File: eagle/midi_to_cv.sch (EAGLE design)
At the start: 46 parts, among them IC1 TL084P, IC2 TL084P, U1 ATMEGA328P_PDIP

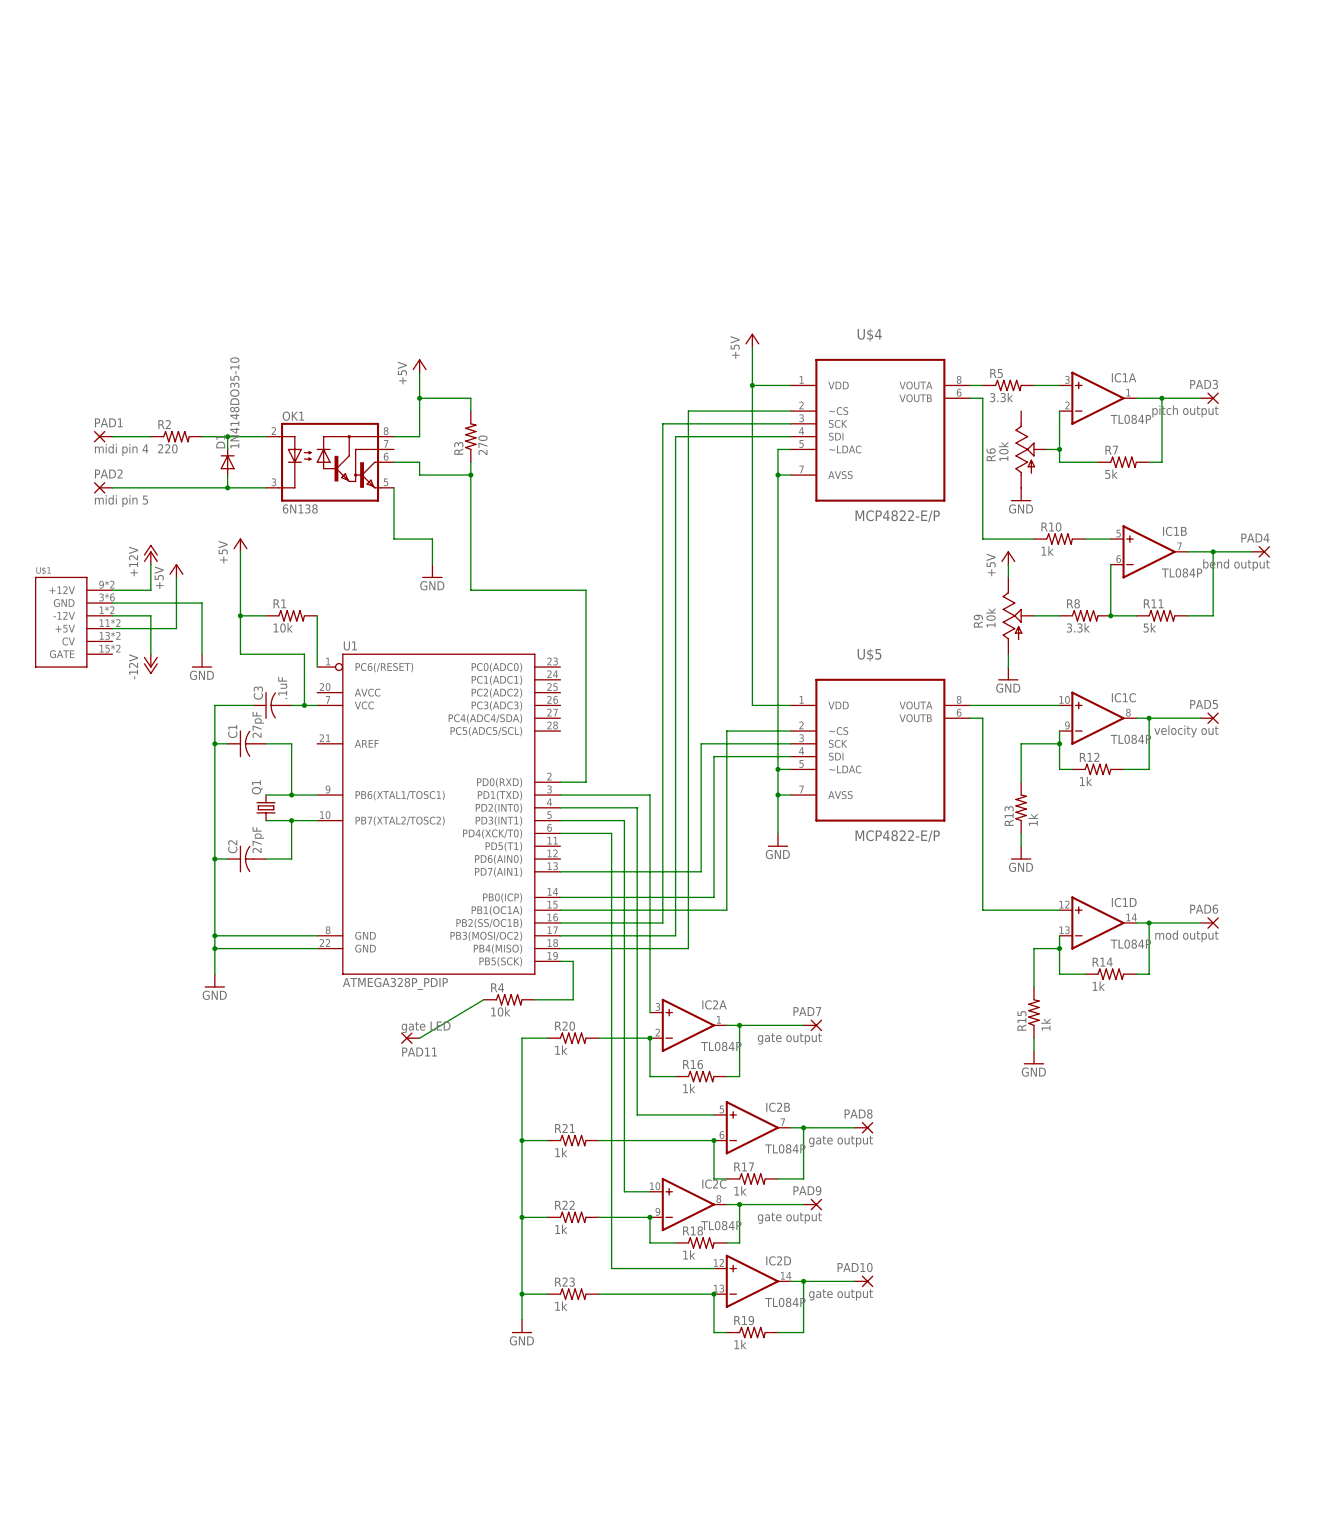
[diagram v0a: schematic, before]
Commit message: power to the op amps
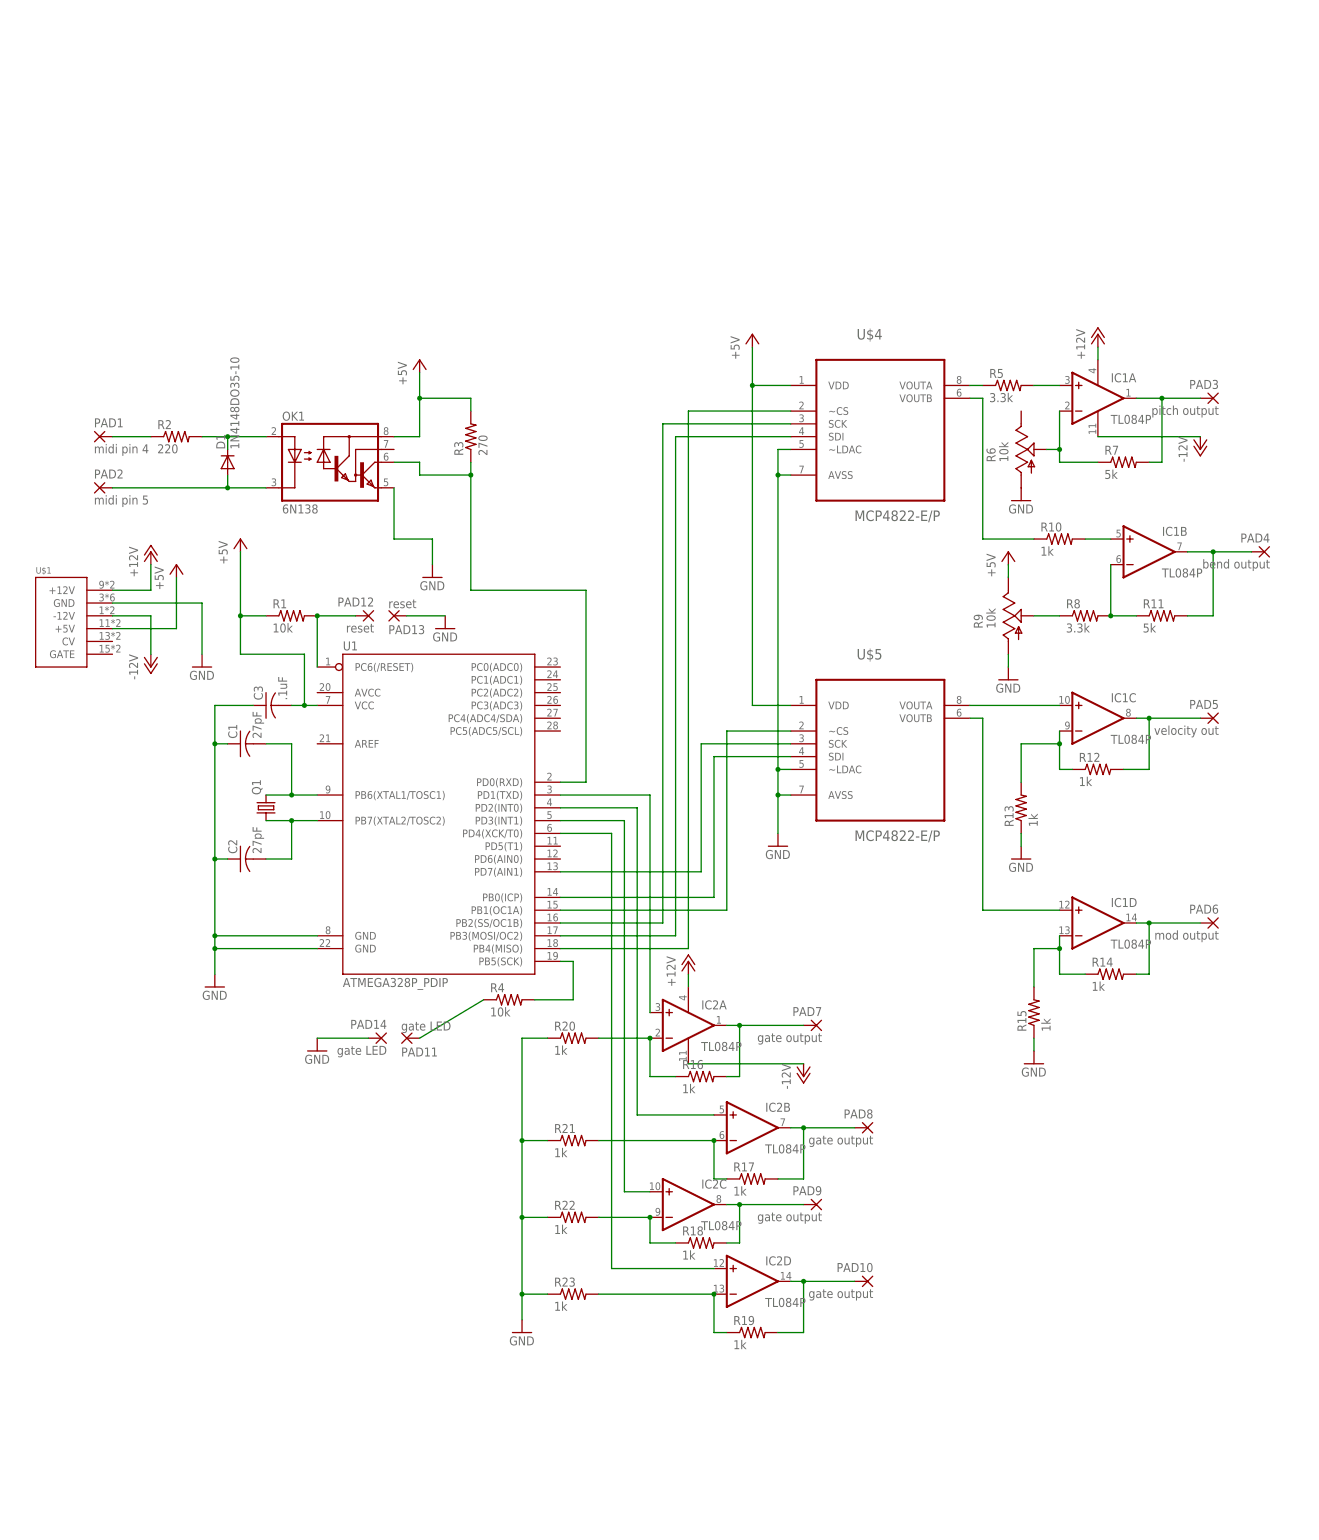
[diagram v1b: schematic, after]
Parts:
- added PAD12, PAD13: reset, wirepad:2,54/0,9
- added PAD14: gate LED, wirepad:2,54/0,9
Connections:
- net +12V: now also IC1P.V+, IC2P.V+
- net -12V: now also IC1P.V-, IC2P.V-
- net GND: now also PAD13.P, PAD14.P
- net N$1: now also PAD12.P
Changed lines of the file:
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@@
 <grid distance="0.1" unitdist="inch" unit="inch" style="lines" multiple="1" display="no" altdistance="0.01" altunitdist="inch" altunit="inch"/>
 <layers>
-<layer number="1" name="Top" color="4" fill="1" visible="no" active="no"/>
-<layer number="16" name="Bottom" color="1" fill="1" visible="no" active="no"/>
-<layer number="17" name="Pads" color="2" fill="1" visible="no" active="no"/>
-<layer number="18" name="Vias" color="2" fill="1" visible="no" active="no"/>
-<layer number="19" name="Unrouted" color="6" fill="1" visible="no" active="no"/>
-<layer number="20" name="Dimension" color="15" fill="1" visible="no" active="no"/>
-<layer number="21" name="tPlace" color="7" fill="1" visible="no" active="no"/>
-<layer number="22" name="bPlace" color="7" fill="1" visible="no" active="no"/>
-<layer number="23" name="tOrigins" color="15" fill="1" visible="no" active="no"/>
-<layer number="24" name="bOrigins" color="15" fill="1" visible="no" active="no"/>
-<layer number="25" name="tNames" color="7" fill="1" visible="no" active="no"/>
-<layer number="26" name="bNames" color="7" fill="1" visible="no" active="no"/>
-<layer number="27" name="tValues" color="7" fill="1" visible="no" active="no"/>
-<layer number="28" name="bValues" color="7" fill="1" visible="no" active="no"/>
+<layer number="1" name="Top" color="4" fill="1" visible="yes" active="no"/>
+<layer number="16" name="Bottom" color="1" fill="1" visible="yes" active="no"/>
+<layer number="17" name="Pads" color="2" fill="1" visible="yes" active="no"/>
+<layer number="18" name="Vias" color="2" fill="1" visible="yes" active="no"/>
+<layer number="19" name="Unrouted" color="6" fill="1" visible="yes" active="no"/>
+<layer number="20" name="Dimension" color="15" fill="1" visible="yes" active="no"/>
+<layer number="21" name="tPlace" color="7" fill="1" visible="yes" active="no"/>
+<layer number="22" name="bPlace" color="7" fill="1" visible="yes" active="no"/>
+<layer number="23" name="tOrigins" color="15" fill="1" visible="yes" active="no"/>
+<layer number="24" name="bOrigins" color="15" fill="1" visible="yes" active="no"/>
+<layer number="25" name="tNames" color="7" fill="1" visible="yes" active="no"/>
+<layer number="26" name="bNames" color="7" fill="1" visible="yes" active="no"/>
+<layer number="27" name="tValues" color="7" fill="1" visible="yes" active="no"/>
+<layer number="28" name="bValues" color="7" fill="1" visible="yes" active="no"/>
 <layer number="29" name="tStop" color="7" fill="3" visible="no" active="no"/>
 <layer number="30" name="bStop" color="7" fill="6" visible="no" active="no"/>
@@
 <layer number="35" name="tGlue" color="7" fill="4" visible="no" active="no"/>
 <layer number="36" name="bGlue" color="7" fill="5" visible="no" active="no"/>
-<layer number="37" name="tTest" color="7" fill="1" visible="no" active="no"/>
-<layer number="38" name="bTest" color="7" fill="1" visible="no" active="no"/>
+<layer number="37" name="tTest" color="7" fill="1" visible="yes" active="no"/>
+<layer number="38" name="bTest" color="7" fill="1" visible="yes" active="no"/>
 <layer number="39" name="tKeepout" color="4" fill="11" visible="no" active="no"/>
 <layer number="40" name="bKeepout" color="1" fill="11" visible="no" active="no"/>
@@
 <layer number="44" name="Drills" color="7" fill="1" visible="no" active="no"/>
 <layer number="45" name="Holes" color="7" fill="1" visible="no" active="no"/>
-<layer number="46" name="Milling" color="3" fill="1" visible="no" active="no"/>
-<layer number="47" name="Measures" color="7" fill="1" visible="no" active="no"/>
-<layer number="48" name="Document" color="7" fill="1" visible="no" active="no"/>
-<layer number="49" name="Reference" color="7" fill="1" visible="no" active="no"/>
-<layer number="50" name="dxf" color="7" fill="1" visible="no" active="no"/>
-<layer number="51" name="tDocu" color="7" fill="1" visible="no" active="no"/>
-<layer number="52" name="bDocu" color="7" fill="1" visible="no" active="no"/>
-<layer number="53" name="tGND_GNDA" color="7" fill="9" visible="no" active="no"/>
-<layer number="54" name="bGND_GNDA" color="1" fill="9" visible="no" active="no"/>
-<layer number="56" name="wert" color="7" fill="1" visible="no" active="no"/>
-<layer number="57" name="tCAD" color="7" fill="1" visible="no" active="no"/>
+<layer number="46" name="Milling" color="3" fill="1" visible="yes" active="no"/>
+<layer number="47" name="Measures" color="7" fill="1" visible="yes" active="no"/>
+<layer number="48" name="Document" color="7" fill="1" visible="yes" active="no"/>
+<layer number="49" name="Reference" color="7" fill="1" visible="yes" active="no"/>
+<layer number="50" name="dxf" color="7" fill="1" visible="yes" active="no"/>
+<layer number="51" name="tDocu" color="7" fill="1" visible="yes" active="no"/>
+<layer number="52" name="bDocu" color="7" fill="1" visible="yes" active="no"/>
+<layer number="53" name="tGND_GNDA" color="7" fill="9" visible="yes" active="no"/>
+<layer number="54" name="bGND_GNDA" color="1" fill="9" visible="yes" active="no"/>
+<layer number="56" name="wert" color="7" fill="1" visible="yes" active="no"/>
+<layer number="57" name="tCAD" color="7" fill="1" visible="yes" active="no"/>
 <layer number="90" name="Modules" color="5" fill="1" visible="yes" active="yes"/>
 <layer number="91" name="Nets" color="2" fill="1" visible="yes" active="yes"/>
@@
 <part name="R22" library="rcl" deviceset="R-US_" device="0207/10" value="1k"/>
 <part name="R23" library="rcl" deviceset="R-US_" device="0207/10" value="1k"/>
+<part name="PAD12" library="wirepad" deviceset="2,54/0,9" device="" value="reset"/>
+<part name="PAD13" library="wirepad" deviceset="2,54/0,9" device="" value="reset "/>
+<part name="GND9" library="supply1" deviceset="GND" device=""/>
+<part name="PAD14" library="wirepad" deviceset="2,54/0,9" device="" value="gate LED"/>
+<part name="GND11" library="supply1" deviceset="GND" device=""/>
+<part name="P-2" library="supply1" deviceset="-12V" device=""/>
+<part name="P-3" library="supply1" deviceset="-12V" device=""/>
+<part name="P+7" library="supply1" deviceset="+12V" device=""/>
+<part name="P+8" library="supply1" deviceset="+12V" device=""/>
 </parts>
 <sheets>
@@
 <instance part="R22" gate="G$1" x="45.72" y="-35.56"/>
 <instance part="R23" gate="G$1" x="45.72" y="-50.8"/>
+<instance part="PAD12" gate="1" x="5.08" y="83.82" rot="MR0"/>
+<instance part="PAD13" gate="1" x="10.16" y="83.82" rot="MR180"/>
+<instance part="GND9" gate="1" x="20.32" y="81.28"/>
+<instance part="PAD14" gate="1" x="7.62" y="0" rot="MR0"/>
+<instance part="GND11" gate="1" x="-5.08" y="-2.54"/>
+<instance part="IC1" gate="P" x="149.86" y="127"/>
+<instance part="P-2" gate="1" x="91.44" y="-7.62"/>
+<instance part="P-3" gate="1" x="170.18" y="116.84"/>
+<instance part="P+7" gate="1" x="149.86" y="139.7"/>
+<instance part="P+8" gate="1" x="68.58" y="15.24"/>
+<instance part="IC2" gate="P" x="68.58" y="2.54"/>
 </instances>
 <busses>
@@
 <pinref part="R1" gate="G$1" pin="2"/>
 <wire x1="-5.08" y1="73.66" x2="-5.08" y2="83.82" width="0.1524" layer="91"/>
+<pinref part="PAD12" gate="1" pin="P"/>
+<wire x1="2.54" y1="83.82" x2="-5.08" y2="83.82" width="0.1524" layer="91"/>
+<junction x="-5.08" y="83.82"/>
 </segment>
 </net>
@@
 <pinref part="R23" gate="G$1" pin="1"/>
 </segment>
+<segment>
+<pinref part="PAD13" gate="1" pin="P"/>
+<pinref part="GND9" gate="1" pin="GND"/>
+<wire x1="12.7" y1="83.82" x2="20.32" y2="83.82" width="0.1524" layer="91"/>
+</segment>
+<segment>
+<wire x1="-5.08" y1="0" x2="5.08" y2="0" width="0.1524" layer="91"/>
+<pinref part="PAD14" gate="1" pin="P"/>
+<pinref part="GND11" gate="1" pin="GND"/>
+</segment>
 </net>
 <net name="+12V" class="0">
@@
 <wire x1="-38.1" y1="88.9" x2="-38.1" y2="93.98" width="0.1524" layer="91"/>
 </segment>
+<segment>
+<pinref part="P+8" gate="1" pin="+12V"/>
+<wire x1="68.58" y1="10.16" x2="68.58" y2="12.7" width="0.1524" layer="91"/>
+<pinref part="IC2" gate="P" pin="V+"/>
+</segment>
+<segment>
+<pinref part="IC1" gate="P" pin="V+"/>
+<pinref part="P+7" gate="1" pin="+12V"/>
+<wire x1="149.86" y1="134.62" x2="149.86" y2="137.16" width="0.1524" layer="91"/>
+</segment>
 </net>
 <net name="-12V" class="0">
@@
 <wire x1="-38.1" y1="83.82" x2="-38.1" y2="76.2" width="0.1524" layer="91"/>
 </segment>
-</net>
+<segment>
+<pinref part="IC1" gate="P" pin="V-"/>
+<pinref part="P-3" gate="1" pin="-12V"/>
+<wire x1="149.86" y1="119.38" x2="170.18" y2="119.38" width="0.1524" layer="91"/>
+</segment>
+<segment>
+<pinref part="IC2" gate="P" pin="V-"/>
+<pinref part="P-2" gate="1" pin="-12V"/>
+<wire x1="68.58" y1="-5.08" x2="91.44" y2="-5.08" width="0.1524" layer="91"/>
+</segment>
+</net>
